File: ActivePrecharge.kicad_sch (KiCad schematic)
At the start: 37 parts, among them IC1 1769205241, J1 Conn_01x03, J2 Conn_01x03, J3 Conn_01x02, Q1 Q_PMOS_GDS, U1 Nucleo_L432KC

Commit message: layout nearly finalized for review
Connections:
- net A_Enable: now also U1.22 (A3)
- net A_Pre_Enable: now also U1.24 (A5)
- net A_Pre_Ready: now also U1.14 (D11)
- net A_Pre_Sense: now also U1.25 (A6)
- net A_Sense: now also U1.23 (A4)
- net CAN_RD: now also U1.18 (AREF); no longer U1.13 (D10)
- net CAN_TD: now also U1.13 (D10); no longer U1.5 (D2)
- net M_Enable: now also U1.20 (A1)
- net M_Pre_Enable: now also U1.16 (D13)
- net M_Pre_Ready: now also U1.15 (D12)
- net M_Pre_Sense: now also U1.19 (A0)
- net M_Sense: now also U1.21 (A2)
- no-connect marks 11 -> 13
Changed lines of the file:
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@@
 	)
 	(no_connect
-		(at 261.62 118.11)
+		(at 236.22 87.63)
 	)
 	(no_connect
-		(at 261.62 107.95)
+		(at 236.22 95.25)
+	)
+	(no_connect
+		(at 236.22 97.79)
 	)
 	(no_connect
@@
 	)
 	(no_connect
-		(at 261.62 97.79)
+		(at 236.22 82.55)
+	)
+	(no_connect
+		(at 236.22 85.09)
 	)
 	(no_connect
-		(at 261.62 110.49)
+		(at 236.22 105.41)
 	)
 	(no_connect
-		(at 261.62 102.87)
+		(at 236.22 107.95)
 	)
 	(no_connect
-		(at 261.62 95.25)
+		(at 236.22 92.71)
 	)
 	(no_connect
-		(at 261.62 113.03)
+		(at 236.22 110.49)
 	)
 	(no_connect
-		(at 261.62 100.33)
+		(at 236.22 100.33)
 	)
 	(no_connect
@@
 	)
 	(no_connect
-		(at 261.62 105.41)
+		(at 236.22 102.87)
 	)
 	(wire
 		(pts
-			(xy 300.99 95.25) (xy 317.5 95.25)
+			(xy 276.86 118.11) (xy 261.62 118.11)
 		)
 		(stroke
@@
 	(wire
 		(pts
+			(xy 228.6 91.44) (xy 228.6 90.17)
+		)
+		(stroke
+			(width 0)
+			(type default)
+		)
+	)
+	(wire
+		(pts
 			(xy 55.88 97.79) (xy 60.96 97.79)
 		)
@@
 	(wire
 		(pts
-			(xy 300.99 115.57) (xy 317.5 115.57)
+			(xy 276.86 95.25) (xy 261.62 95.25)
 		)
 		(stroke
@@
 	(wire
 		(pts
-			(xy 275.59 85.09) (xy 275.59 88.9)
+			(xy 275.59 85.09) (xy 275.59 86.36)
 		)
 		(stroke
@@
 	(wire
 		(pts
-			(xy 261.62 115.57) (xy 271.78 115.57)
+			(xy 261.62 115.57) (xy 276.86 115.57)
 		)
 		(stroke
@@
 	(wire
 		(pts
-			(xy 214.63 90.17) (xy 236.22 90.17)
+			(xy 36.83 77.47) (xy 48.26 77.47)
 		)
 		(stroke
@@
 	(wire
 		(pts
-			(xy 36.83 77.47) (xy 48.26 77.47)
+			(xy 250.19 34.29) (xy 250.19 36.83)
 		)
 		(stroke
@@
 	(wire
 		(pts
-			(xy 250.19 34.29) (xy 250.19 36.83)
+			(xy 142.24 173.99) (xy 151.13 173.99)
 		)
 		(stroke
@@
 	(wire
 		(pts
-			(xy 142.24 173.99) (xy 151.13 173.99)
+			(xy 36.83 87.63) (xy 48.26 87.63)
 		)
 		(stroke
@@
 	(wire
 		(pts
-			(xy 36.83 87.63) (xy 48.26 87.63)
+			(xy 102.87 55.88) (xy 114.3 55.88)
 		)
 		(stroke
@@
 	(wire
 		(pts
-			(xy 102.87 55.88) (xy 114.3 55.88)
+			(xy 148.59 95.25) (xy 148.59 102.87)
 		)
 		(stroke
@@
 	(wire
 		(pts
-			(xy 148.59 95.25) (xy 148.59 102.87)
+			(xy 228.6 90.17) (xy 236.22 90.17)
 		)
 		(stroke
@@
 	(wire
 		(pts
-			(xy 300.99 83.82) (xy 317.5 83.82)
+			(xy 220.98 118.11) (xy 236.22 118.11)
 		)
 		(stroke
@@
 	(wire
 		(pts
-			(xy 300.99 113.03) (xy 317.5 113.03)
+			(xy 276.86 105.41) (xy 261.62 105.41)
 		)
 		(stroke
@@
 	(wire
 		(pts
-			(xy 300.99 102.87) (xy 317.5 102.87)
+			(xy 276.86 102.87) (xy 261.62 102.87)
 		)
 		(stroke
@@
 	(wire
 		(pts
-			(xy 227.33 92.71) (xy 236.22 92.71)
+			(xy 220.98 113.03) (xy 236.22 113.03)
 		)
 		(stroke
@@
 	(wire
 		(pts
-			(xy 227.33 113.03) (xy 236.22 113.03)
+			(xy 276.86 113.03) (xy 261.62 113.03)
 		)
 		(stroke
@@
 	(wire
 		(pts
-			(xy 317.5 86.36) (xy 300.99 86.36)
+			(xy 236.22 115.57) (xy 220.98 115.57)
 		)
 		(stroke
@@
 	(wire
 		(pts
-			(xy 300.99 110.49) (xy 317.5 110.49)
+			(xy 276.86 110.49) (xy 261.62 110.49)
 		)
 		(stroke
@@
 	(wire
 		(pts
-			(xy 300.99 118.11) (xy 317.5 118.11)
+			(xy 276.86 100.33) (xy 261.62 100.33)
 		)
 		(stroke
@@
 	(wire
 		(pts
-			(xy 300.99 97.79) (xy 317.5 97.79)
+			(xy 276.86 97.79) (xy 261.62 97.79)
 		)
 		(stroke
@@
 	(wire
 		(pts
-			(xy 300.99 100.33) (xy 317.5 100.33)
+			(xy 276.86 107.95) (xy 261.62 107.95)
 		)
 		(stroke
@@
 	)
 	(label "3V3"
-		(at 271.78 115.57 180)
+		(at 276.86 115.57 180)
 		(fields_autoplaced yes)
 		(effects
@@
 	)
 	(label "M_Pre_Sense"
-		(at 300.99 110.49 0)
+		(at 276.86 110.49 180)
 		(fields_autoplaced yes)
 		(effects
@@
 				(size 1.27 1.27)
 			)
-			(justify left bottom)
+			(justify right bottom)
 		)
 	)
@@
 	)
 	(label "M_Enable"
-		(at 300.99 100.33 0)
+		(at 276.86 107.95 180)
 		(fields_autoplaced yes)
 		(effects
@@
 				(size 1.27 1.27)
 			)
-			(justify left bottom)
+			(justify right bottom)
 		)
 	)
@@
 	)
 	(label "CAN_TD"
-		(at 227.33 92.71 0)
+		(at 220.98 113.03 0)
 		(fields_autoplaced yes)
 		(effects
@@
 	)
 	(label "A_Enable"
-		(at 300.99 102.87 0)
+		(at 276.86 102.87 180)
 		(fields_autoplaced yes)
 		(effects
@@
 				(size 1.27 1.27)
 			)
-			(justify left bottom)
+			(justify right bottom)
 		)
 	)
@@
 	)
 	(label "A_Pre_Ready"
-		(at 300.99 86.36 0)
+		(at 220.98 115.57 0)
 		(fields_autoplaced yes)
 		(effects
@@
 	)
 	(label "A_Pre_Enable"
-		(at 300.99 97.79 0)
+		(at 276.86 97.79 180)
 		(fields_autoplaced yes)
 		(effects
@@
 				(size 1.27 1.27)
 			)
-			(justify left bottom)
+			(justify right bottom)
 		)
 	)
@@
 	)
 	(label "A_Pre_Sense"
-		(at 300.99 115.57 0)
+		(at 276.86 95.25 180)
 		(fields_autoplaced yes)
 		(effects
@@
 				(size 1.27 1.27)
 			)
-			(justify left bottom)
+			(justify right bottom)
 		)
 	)
@@
 	)
 	(label "M_Pre_Ready"
-		(at 300.99 83.82 0)
+		(at 220.98 118.11 0)
 		(fields_autoplaced yes)
 		(effects
@@
 	)
 	(label "A_Sense"
-		(at 300.99 118.11 0)
+		(at 276.86 100.33 180)
 		(fields_autoplaced yes)
 		(effects
@@
 				(size 1.27 1.27)
 			)
-			(justify left bottom)
+			(justify right bottom)
 		)
 	)
@@
 	)
 	(label "CAN_RD"
-		(at 227.33 113.03 0)
+		(at 276.86 113.03 180)
 		(fields_autoplaced yes)
 		(effects
@@
 				(size 1.27 1.27)
 			)
-			(justify left bottom)
+			(justify right bottom)
 		)
 	)
@@
 	)
 	(label "M_Sense"
-		(at 300.99 113.03 0)
+		(at 276.86 105.41 180)
 		(fields_autoplaced yes)
 		(effects
@@
 				(size 1.27 1.27)
 			)
-			(justify left bottom)
+			(justify right bottom)
 		)
 	)
@@
 	)
 	(label "M_Pre_Enable"
-		(at 300.99 95.25 0)
+		(at 276.86 118.11 180)
 		(fields_autoplaced yes)
 		(effects
@@
 				(size 1.27 1.27)
 			)
-			(justify left bottom)
+			(justify right bottom)
 		)
 	)
@@
 	(symbol
 		(lib_id "power:GND")
-		(at 214.63 90.17 0)
+		(at 228.6 91.44 0)
 		(unit 1)
 		(exclude_from_sim no)
@@
 		(fields_autoplaced yes)
 		(property "Reference" "#PWR06"
-			(at 214.63 96.52 0)
+			(at 228.6 97.79 0)
 			(effects
 				(font
@@
 		)
 		(property "Value" "LVGND"
-			(at 214.63 95.25 0)
+			(at 228.6 96.52 0)
 			(effects
 				(font
@@
 		)
 		(property "Footprint" ""
-			(at 214.63 90.17 0)
+			(at 228.6 91.44 0)
 			(effects
 				(font
@@
 		)
 		(property "Datasheet" ""
-			(at 214.63 90.17 0)
+			(at 228.6 91.44 0)
 			(effects
 				(font
@@
 		)
 		(property "Description" "Power symbol creates a global label with name \"GND\" , ground"
-			(at 214.63 90.17 0)
+			(at 228.6 91.44 0)
 			(effects
 				(font
@@
 	(symbol
 		(lib_id "power:GND")
-		(at 275.59 88.9 0)
+		(at 275.59 86.36 0)
 		(unit 1)
 		(exclude_from_sim no)
@@
 		(fields_autoplaced yes)
 		(property "Reference" "#PWR013"
-			(at 275.59 95.25 0)
+			(at 275.59 92.71 0)
 			(effects
 				(font
@@
 		)
 		(property "Value" "LVGND"
-			(at 275.59 93.98 0)
+			(at 275.59 91.44 0)
 			(effects
 				(font
@@
 		)
 		(property "Footprint" ""
-			(at 275.59 88.9 0)
+			(at 275.59 86.36 0)
 			(effects
 				(font
@@
 		)
 		(property "Datasheet" ""
-			(at 275.59 88.9 0)
+			(at 275.59 86.36 0)
 			(effects
 				(font
@@
 		)
 		(property "Description" "Power symbol creates a global label with name \"GND\" , ground"
-			(at 275.59 88.9 0)
+			(at 275.59 86.36 0)
 			(effects
 				(font

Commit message: layout review fixes
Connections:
- net CAN_RD: now also U1.13 (D10); no longer U1.18 (AREF)
- net CAN_TD: now also U1.5 (D2); no longer U1.13 (D10)
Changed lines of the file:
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@@
 	)
 	(no_connect
-		(at 236.22 105.41)
+		(at 261.62 113.03)
 	)
 	(no_connect
-		(at 236.22 107.95)
+		(at 236.22 105.41)
 	)
 	(no_connect
-		(at 236.22 92.71)
+		(at 236.22 107.95)
 	)
 	(no_connect
@@
 	(wire
 		(pts
-			(xy 228.6 91.44) (xy 228.6 90.17)
+			(xy 217.17 91.44) (xy 217.17 90.17)
 		)
 		(stroke
@@
 	(wire
 		(pts
+			(xy 220.98 92.71) (xy 236.22 92.71)
+		)
+		(stroke
+			(width 0)
+			(type default)
+		)
+	)
+	(wire
+		(pts
 			(xy 152.4 62.23) (xy 152.4 60.96)
 		)
@@
 	(wire
 		(pts
-			(xy 228.6 90.17) (xy 236.22 90.17)
+			(xy 217.17 90.17) (xy 236.22 90.17)
 		)
 		(stroke
@@
 	(wire
 		(pts
+			(xy 220.98 113.03) (xy 236.22 113.03)
+		)
+		(stroke
+			(width 0)
+			(type default)
+		)
+	)
+	(wire
+		(pts
 			(xy 194.31 102.87) (xy 187.96 102.87)
 		)
@@
 	(wire
 		(pts
-			(xy 220.98 113.03) (xy 236.22 113.03)
-		)
-		(stroke
-			(width 0)
-			(type default)
-		)
-	)
-	(wire
-		(pts
-			(xy 276.86 113.03) (xy 261.62 113.03)
-		)
-		(stroke
-			(width 0)
-			(type default)
-		)
-	)
-	(wire
-		(pts
 			(xy 25.4 27.94) (xy 36.83 27.94)
 		)
@@
 	)
 	(label "CAN_TD"
-		(at 220.98 113.03 0)
-		(fields_autoplaced yes)
-		(effects
-			(font
-				(size 1.27 1.27)
-			)
-			(justify left bottom)
-		)
-	)
-	(label "CAN_TD"
 		(at 142.24 168.91 0)
 		(fields_autoplaced yes)
@@
 		)
 	)
+	(label "CAN_RD"
+		(at 220.98 113.03 0)
+		(fields_autoplaced yes)
+		(effects
+			(font
+				(size 1.27 1.27)
+			)
+			(justify left bottom)
+		)
+	)
 	(label "M_Pre_Enable"
 		(at 194.31 110.49 0)
@@
 		)
 	)
+	(label "CAN_TD"
+		(at 220.98 92.71 0)
+		(fields_autoplaced yes)
+		(effects
+			(font
+				(size 1.27 1.27)
+			)
+			(justify left bottom)
+		)
+	)
 	(label "A_Sense"
 		(at 276.86 100.33 180)
@@
 		)
 	)
-	(label "CAN_RD"
-		(at 276.86 113.03 180)
-		(fields_autoplaced yes)
-		(effects
-			(font
-				(size 1.27 1.27)
-			)
-			(justify right bottom)
-		)
-	)
 	(label "A_Enable"
 		(at 194.31 118.11 0)
@@
 	(symbol
 		(lib_id "power:GND")
-		(at 228.6 91.44 0)
+		(at 217.17 91.44 0)
 		(unit 1)
 		(exclude_from_sim no)
@@
 		(fields_autoplaced yes)
 		(property "Reference" "#PWR06"
-			(at 228.6 97.79 0)
+			(at 217.17 97.79 0)
 			(effects
 				(font
@@
 		)
 		(property "Value" "LVGND"
-			(at 228.6 96.52 0)
+			(at 217.17 96.52 0)
 			(effects
 				(font
@@
 		)
 		(property "Footprint" ""
-			(at 228.6 91.44 0)
+			(at 217.17 91.44 0)
 			(effects
 				(font
@@
 		)
 		(property "Datasheet" ""
-			(at 228.6 91.44 0)
+			(at 217.17 91.44 0)
 			(effects
 				(font
@@
 		)
 		(property "Description" "Power symbol creates a global label with name \"GND\" , ground"
-			(at 228.6 91.44 0)
+			(at 217.17 91.44 0)
 			(effects
 				(font

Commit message: initial commit v2
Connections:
- net A_Enable: no longer names the net of U1.22 (A3)
- net A_Sense: no longer names the net of U1.23 (A4)
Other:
- sheet Contactor Drivers ports: added none; removed A_Enable, A_Sense
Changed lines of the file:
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@@
 	(wire
 		(pts
-			(xy 187.96 134.62) (xy 194.31 134.62)
-		)
-		(stroke
-			(width 0)
-			(type default)
-		)
-	)
-	(wire
-		(pts
 			(xy 276.86 95.25) (xy 261.62 95.25)
 		)
@@
 	(wire
 		(pts
-			(xy 276.86 102.87) (xy 261.62 102.87)
-		)
-		(stroke
-			(width 0)
-			(type default)
-		)
-	)
-	(wire
-		(pts
 			(xy 203.2 40.64) (xy 213.36 40.64)
 		)
@@
 	(wire
 		(pts
-			(xy 187.96 118.11) (xy 194.31 118.11)
-		)
-		(stroke
-			(width 0)
-			(type default)
-		)
-	)
-	(wire
-		(pts
 			(xy 234.95 48.26) (xy 234.95 49.53)
 		)
@@
 	(wire
 		(pts
-			(xy 276.86 100.33) (xy 261.62 100.33)
-		)
-		(stroke
-			(width 0)
-			(type default)
-		)
-	)
-	(wire
-		(pts
 			(xy 25.4 44.45) (xy 36.83 44.45)
 		)
@@
 		)
 	)
-	(label "A_Enable"
-		(at 276.86 102.87 180)
-		(fields_autoplaced yes)
-		(effects
-			(font
-				(size 1.27 1.27)
-			)
-			(justify right bottom)
-		)
-	)
 	(label "5V"
 		(at 270.51 90.17 180)
@@
 		)
 	)
-	(label "A_Sense"
-		(at 276.86 100.33 180)
-		(fields_autoplaced yes)
-		(effects
-			(font
-				(size 1.27 1.27)
-			)
-			(justify right bottom)
-		)
-	)
 	(label "Array HVRef"
 		(at 82.55 87.63 180)
@@
 		)
 	)
-	(label "A_Enable"
-		(at 194.31 118.11 0)
-		(fields_autoplaced yes)
-		(effects
-			(font
-				(size 1.27 1.27)
-			)
-			(justify left bottom)
-		)
-	)
 	(label "ISO_PWR"
 		(at 78.74 120.65 0)
@@
 		)
 	)
-	(label "A_Sense"
-		(at 194.31 134.62 0)
-		(fields_autoplaced yes)
-		(effects
-			(font
-				(size 1.27 1.27)
-			)
-			(justify left bottom)
-		)
-	)
 	(label "HVGND"
 		(at 87.63 31.75 180)
@@
 			)
 		)
-		(pin "A_Enable" input
-			(at 187.96 118.11 0)
-			(effects
-				(font
-					(size 1.27 1.27)
-				)
-				(justify right)
-			)
-		)
 		(pin "M_Pre_Sense" output
 			(at 187.96 127 0)
@@
 			(effects
 				(font
-					(size 1.27 1.27)
-				)
-				(justify right)
-			)
-		)
-		(pin "A_Sense" output
-			(at 187.96 134.62 0)
-			(effects
-				(font

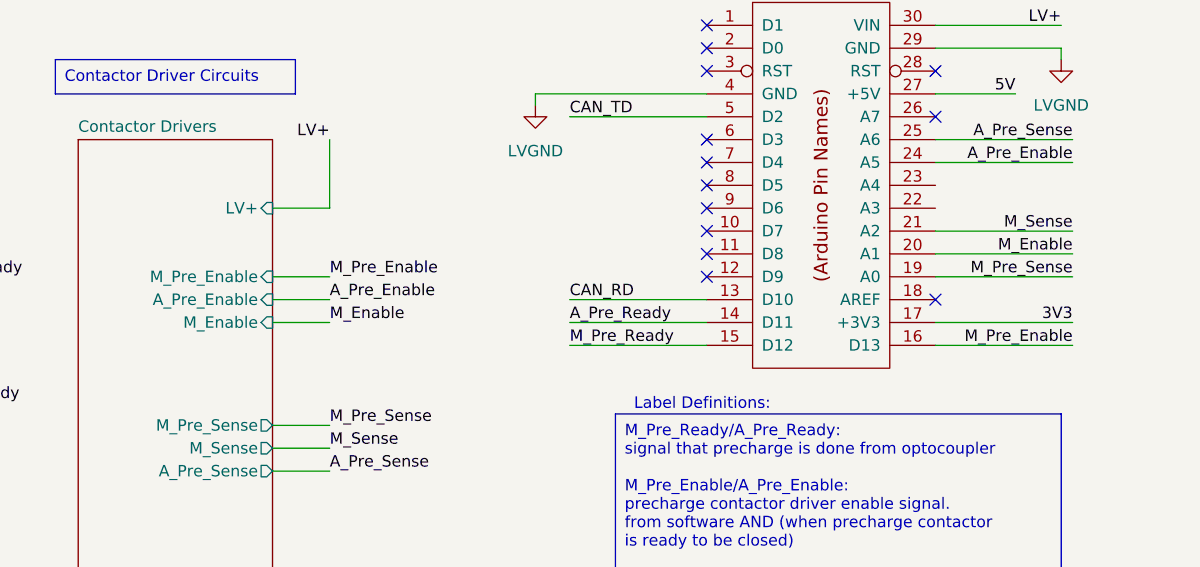
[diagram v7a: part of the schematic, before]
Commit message: fixed HV layout and added the both nmos
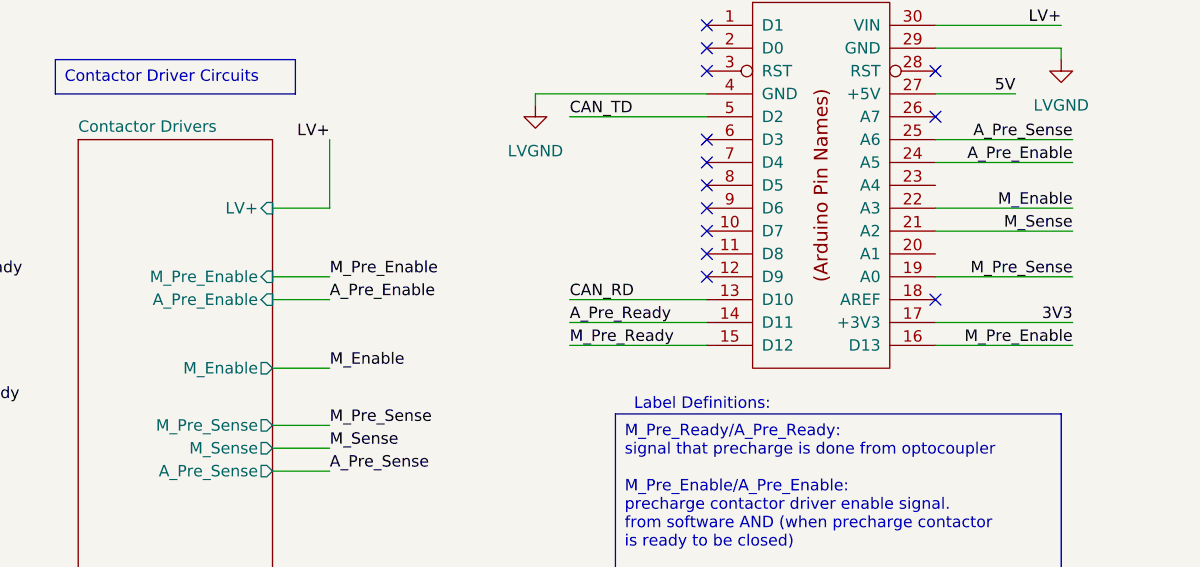
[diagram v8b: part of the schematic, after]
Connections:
- net M_Enable: now also U1.22 (A3); no longer U1.20 (A1)
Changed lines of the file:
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@@
 	(wire
 		(pts
+			(xy 261.62 102.87) (xy 276.86 102.87)
+		)
+		(stroke
+			(width 0)
+			(type default)
+		)
+	)
+	(wire
+		(pts
 			(xy 107.95 114.3) (xy 120.65 114.3)
 		)
@@
 	(wire
 		(pts
-			(xy 187.96 115.57) (xy 194.31 115.57)
+			(xy 187.96 120.65) (xy 194.31 120.65)
 		)
 		(stroke
@@
 		)
 	)
-	(wire
-		(pts
-			(xy 276.86 107.95) (xy 261.62 107.95)
-		)
-		(stroke
-			(width 0)
-			(type default)
-		)
-	)
 	(rectangle
 		(start 358.394 127.762)
@@
 		)
 	)
-	(label "M_Enable"
-		(at 276.86 107.95 180)
-		(fields_autoplaced yes)
-		(effects
-			(font
-				(size 1.27 1.27)
-			)
-			(justify right bottom)
-		)
-	)
 	(label "Motor HRef"
 		(at 36.83 27.94 180)
@@
 	)
 	(label "M_Enable"
-		(at 194.31 115.57 0)
+		(at 194.31 120.65 0)
 		(fields_autoplaced yes)
 		(effects
@@
 		)
 	)
+	(label "M_Enable"
+		(at 276.86 102.87 180)
+		(fields_autoplaced yes)
+		(effects
+			(font
+				(size 1.27 1.27)
+			)
+			(justify right bottom)
+		)
+	)
 	(symbol
 		(lib_id "Device:Fuse")
@@
 			)
 		)
-		(pin "M_Enable" input
-			(at 187.96 115.57 0)
+		(pin "A_Pre_Enable" input
+			(at 187.96 113.03 0)
 			(effects
 				(font
@@
 			)
 		)
-		(pin "A_Pre_Enable" input
-			(at 187.96 113.03 0)
+		(pin "M_Pre_Enable" input
+			(at 187.96 110.49 0)
 			(effects
 				(font
@@
 			)
 		)
-		(pin "M_Pre_Enable" input
-			(at 187.96 110.49 0)
+		(pin "M_Enable" output
+			(at 187.96 120.65 0)
 			(effects
 				(font
